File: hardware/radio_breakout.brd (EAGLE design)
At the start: 21.5 x 31.4 mm, 14 parts

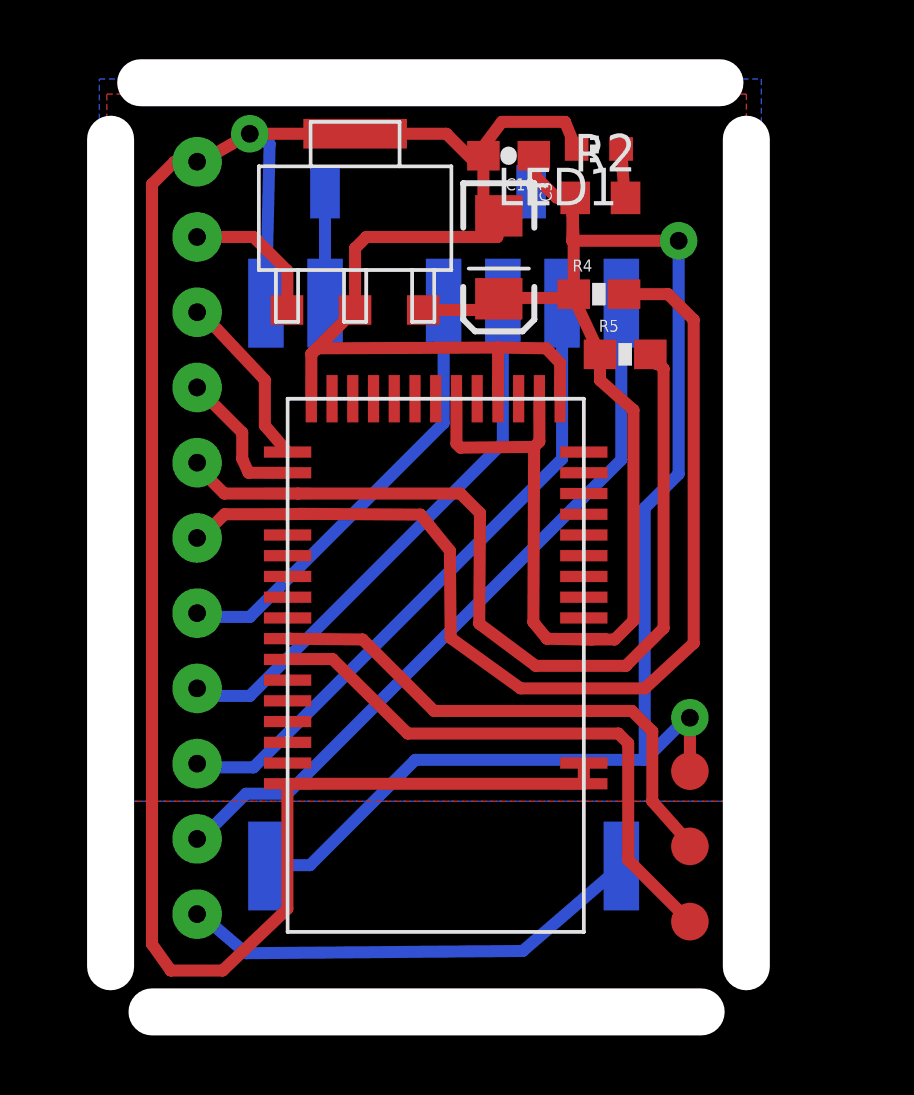
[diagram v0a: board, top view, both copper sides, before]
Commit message: replaced UART with SPI bluefruit software and hardware
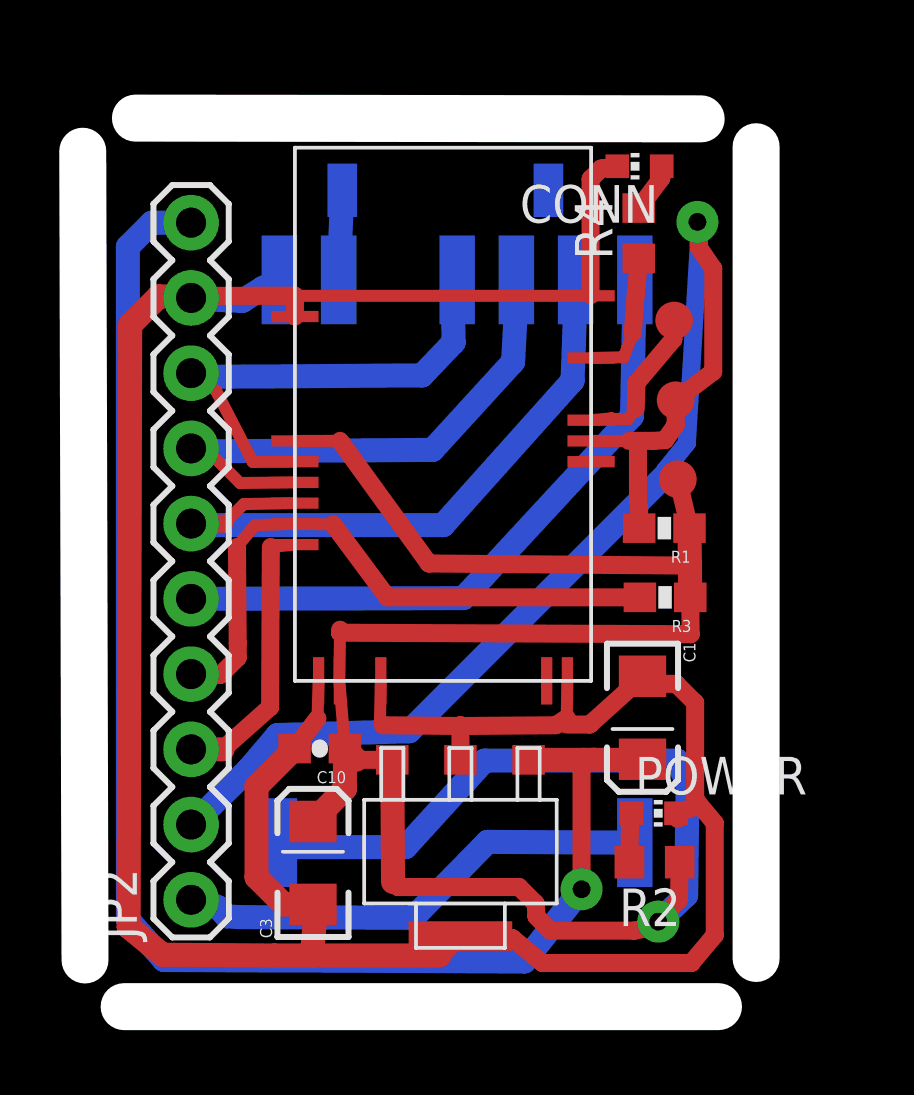
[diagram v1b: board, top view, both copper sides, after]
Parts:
- removed DATA: PAD, ITP_Lab:SMD-ROUND
- removed LED1: (no value), adafruit:CHIP-LED0603
- removed R5: 100k, SparkFun-Resistors:0603-RES
- removed U$4: MDBT40, ITP_Lab:MDBT40
- added C1: 10uF, SparkFun-Capacitors:EIA3216
- added CLOCK1: PAD, ITP_Lab:SMD-ROUND
- added CONN, POWER: (no value), adafruit:CHIP-LED0603
- added JP2: M10", SparkFun-Connectors:1X10
- added R1, R3: 10k, SparkFun-Resistors:0603-RES
- C10: value 0.1uF -> 1uF
- R2: value (none) -> 10k
- R4: value 100k -> 10k; device SparkFun-Resistors:0603-RES -> adafruit:R0603
- U$5: value HEADER-11 -> NRF51-MDBT40-SPI; device ITP_Lab:HEADER-11 -> ITP_Lab:SOC-NRF51-MDBT40-SPI
- moved R2 22.5 mm to (18.0, 4.29), turned to 180 degrees
- moved U$3 21.7 mm to (11.4, 4.65), turned to 180 degrees
- moved C3 21.4 mm to (6.45, 4.27), turned to 90 degrees
- moved C10 21.0 mm to (6.68, 8.13)
- moved CLOCK 20.3 mm to (18.6, 22.6), turned to 180 degrees
- moved VCC 9.86 mm to (18.8, 17.2), turned to 180 degrees
- moved U$5 8.84 mm to (10.9, 18.0), turned to 0 degrees
- moved R4 2.46 mm to (17.4, 25.5), turned to 90 degrees
- moved U$1 0.91 mm to (12.3, 14.5)
- moved U$2 0.59 mm to (10.9, 27.0)
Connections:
- removed net BT-CTS: R5.2, U$4.P0.10, U$5.5
- removed net BT-RTS: U$4.P0.08, U$5.3
- removed net BT-RX: R4.2, U$4.P0.11, U$5.6
- removed net BT-TX: U$4.P0.09, U$5.4
- removed net N$12: DATA.P$1, U$4.SWDIO
- new net BT-REQ: JP2.3, U$5.P0.25
- new net BT-SS: JP2.4, R3.2, U$5.P0.24
- new net N$2: R4.1, U$5.P0.19
- new net N$4: CONN.A, R4.2
- new net SWDIO/RST: CLOCK1.P$1, JP2.2, R1.2, U$5.SWDIO
- net GND: now also C1.C, CONN.C, JP2.9, POWER.C, U$5.GND1, U$5.GND2, U$5.GND3, U$5.GND4, U$5.GND5, U$5.P0.30; no longer LED1.C, U$4.GND1, U$4.GND2, U$4.GND3, U$4.GND4, U$4.GND5, U$4.P0.30, U$5.1
- net MISO: now also JP2.7, U$5.P0.22; no longer U$5.8
- net MOSI: now also JP2.6, U$5.P0.23; no longer U$5.9
- net N$1: now also POWER.A; no longer LED1.A
- net N$11: now also U$5.SWCLK; no longer U$4.SWCLK
- net RF-REQ: now also JP2.1; no longer U$5.11
- net RF-SS: now also JP2.5; no longer U$5.10
- net SCK: now also JP2.8, U$5.P0.21; no longer U$5.7
- net VCC: now also R1.1, R3.1, U$5.AVDD, U$5.VDD; no longer R4.1, R5.1, U$4.AVDD, U$4.P0.01, U$4.VDD
- net VIN: now also C1.A, JP2.10; no longer U$5.2
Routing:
- net VIN: track 4.85 -> 51.5 mm, vias 0 -> 1
- net SWDIO/RST: track 0.00 -> 43.6 mm, vias 0 -> 1
- net BT-RX: track 35.4 -> 0.00 mm
- net BT-CTS: track 30.7 -> 0.00 mm
- net BT-SS: track 0.00 -> 20.8 mm
- net N$12: track 17.9 -> 0.00 mm
- net N$11: track 19.6 -> 5.13 mm
- net BT-REQ: track 0.00 -> 9.59 mm
- net GND: track 95.5 -> 103.4 mm, vias 1 -> 0
- net BT-RTS: track 5.99 -> 0.00 mm
- net BT-TX: track 4.88 -> 0.00 mm
- net N$2: track 0.00 -> 4.57 mm
- net RF-SS: track 24.9 -> 22.2 mm
- net N$4: track 0.00 -> 1.68 mm
- net SCK: track 15.1 -> 16.7 mm
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- removed copper zone on layer 1, net GND
- removed copper zone on layer 16, net GND
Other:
- board size 21.5 x 31.4 mm -> 22.7 x 30 mm

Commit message: update board files, arduino library, and readme
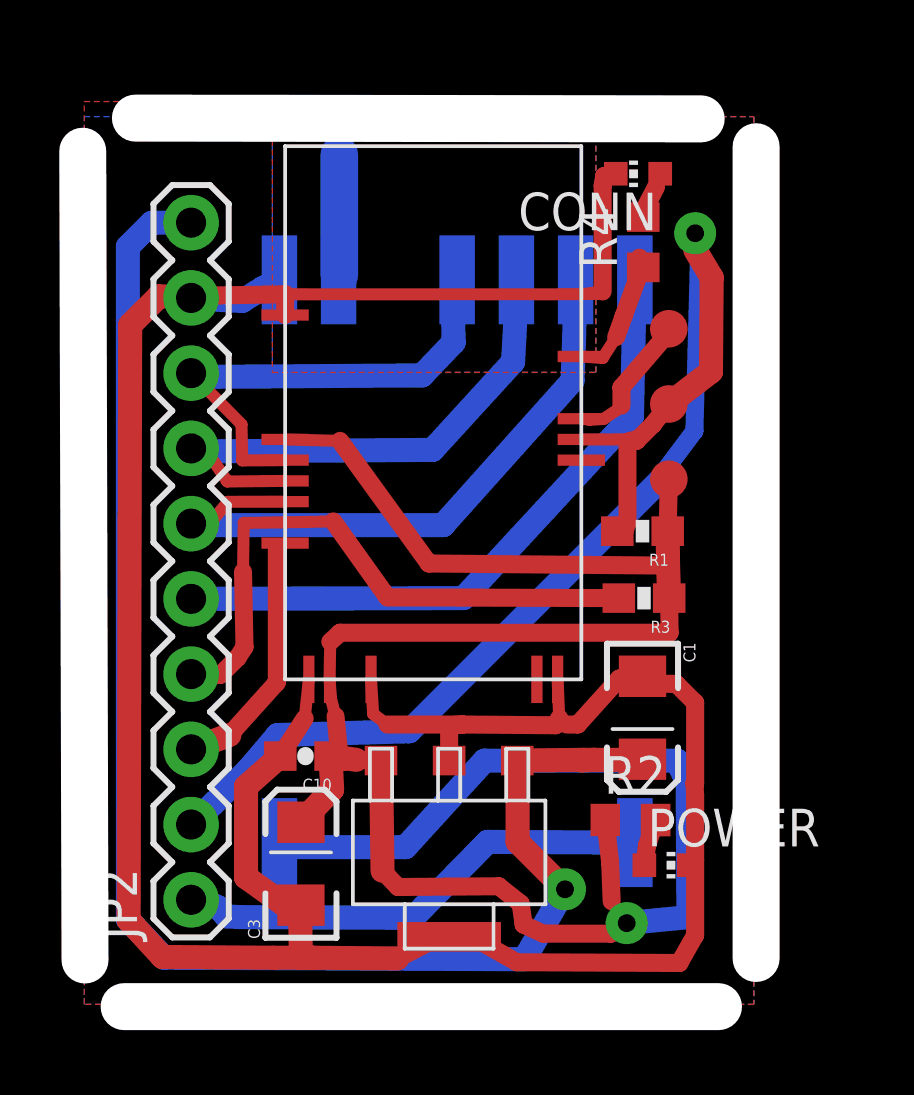
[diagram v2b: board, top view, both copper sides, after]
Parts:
- removed U$2: 915MHZ-ANTENNA-SMD, ITP_Lab:915MHZ-ANTENNA
- moved POWER 1.81 mm to (18.4, 4.19)
- moved R2 1.64 mm to (17.2, 5.71), turned to 0 degrees
- moved R1 0.74 mm to (17.6, 15.5)
- moved R3 0.71 mm to (17.6, 13.2)
- moved C10 0.55 mm to (6.20, 7.87)
- moved C3 0.41 mm to (6.05, 4.24)
- moved U$3 0.38 mm to (11.0, 4.62)
- moved R4 0.34 mm to (17.6, 25.2)
- moved U$5 0.33 mm to (10.6, 18.1)
- moved CLOCK 0.33 mm to (18.5, 22.3)
- moved VCC 0.30 mm to (18.5, 17.2)
- moved CLOCK1 0.26 mm to (18.5, 19.8)
- moved CONN 0.26 mm to (17.4, 27.5)
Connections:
- removed net N$6: U$1.ANT, U$2.SIGNAL
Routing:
- net VIN: track 51.5 -> 54.3 mm
- net GND: track 103.4 -> 101.9 mm
- net N$6: track 3.02 -> 4.06 mm
- net VCC: track 78.4 -> 79.4 mm
- net BT-REQ: track 9.59 -> 8.81 mm
- added copper zone on layer 1, net GND
- added copper zone on layer 16, net GND
